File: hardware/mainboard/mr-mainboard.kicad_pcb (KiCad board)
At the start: 0 parts

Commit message: First pass at placement
Signed-off-by: David Shah <dave@ds0.me>
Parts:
- added C1: 470n, Capacitor_SMD:C_0402_1005Metric, F.Cu at (95.8, 152.2)
- added C10: 10µ, Capacitor_SMD:C_0805_2012Metric, B.Cu at (113.8, 130.0)
- added C11: 470n, Capacitor_SMD:C_0402_1005Metric, F.Cu at (89.3, 150.8)
- added C12: 10µ, Capacitor_SMD:C_0805_2012Metric, B.Cu at (113.8, 132.2)
- added C13: 10µ, Capacitor_SMD:C_0805_2012Metric, B.Cu at (113.8, 139.0)
- added C14: 10µ, Capacitor_SMD:C_0805_2012Metric, B.Cu at (81.8, 132.0)
- added C15: 10µ, Capacitor_SMD:C_0805_2012Metric, B.Cu at (83.5, 155.0)
- added C16: 10µ, Capacitor_SMD:C_0805_2012Metric, B.Cu at (81.0, 161.5)
- added C17: 10µ, Capacitor_SMD:C_0805_2012Metric, B.Cu at (83.8, 161.5)
- added C18: 10µ, Capacitor_SMD:C_0805_2012Metric, B.Cu at (92.5, 161.5)
- added C19: 10µ, Capacitor_SMD:C_0805_2012Metric, B.Cu at (86.5, 161.5)
- added C2: 470n, Capacitor_SMD:C_0402_1005Metric, F.Cu at (93.8, 152.2)
- added C20: 10µ, Capacitor_SMD:C_0805_2012Metric, B.Cu at (89.5, 161.5)
- added C21: 100n, Capacitor_SMD:C_0402_1005Metric, F.Cu at (87.8, 153.7)
- added C22: 100n, Capacitor_SMD:C_0402_1005Metric, F.Cu at (89.5, 155.8)
- added C23: 100n, Capacitor_SMD:C_0402_1005Metric, F.Cu at (90.7, 155.7)
- added C24: 100n, Capacitor_SMD:C_0402_1005Metric, F.Cu at (92.0, 155.8)
- added C25: 100n, Capacitor_SMD:C_0402_1005Metric, F.Cu at (91.0, 153.8)
- added C26: 100n, Capacitor_SMD:C_0402_1005Metric, F.Cu at (93.5, 154.5)
- added C27: 10µ, Capacitor_SMD:C_0805_2012Metric, B.Cu at (65.8, 183.0)
- added C28: 10µ, Capacitor_SMD:C_0805_2012Metric, B.Cu at (66.0, 171.8)
- added C29: 10µ, Capacitor_SMD:C_0805_2012Metric, B.Cu at (63.2, 171.8)
- added C3: 470n, Capacitor_SMD:C_0402_1005Metric, F.Cu at (94.2, 149.0)
- added C30: 100n, Capacitor_SMD:C_0402_1005Metric, F.Cu at (100.8, 149.8)
- added C31: 100n, Capacitor_SMD:C_0402_1005Metric, B.Cu at (76.3, 177.8)
- added C32: 1µ, Capacitor_SMD:C_0603_1608Metric, B.Cu at (82.5, 176.5)
- added C33: 1µ, Capacitor_SMD:C_0603_1608Metric, B.Cu at (82.5, 170.0)
- added C34: 10µ, Capacitor_SMD:C_0805_2012Metric, B.Cu at (79.0, 181.0)
- added C35: 10µ, Capacitor_SMD:C_0805_2012Metric, B.Cu at (75.0, 172.2)
- added C36: 10µ, Capacitor_SMD:C_0805_2012Metric, B.Cu at (65.8, 180.8)
- added C37: 10µ, Capacitor_SMD:C_0805_2012Metric, B.Cu at (79.0, 183.2)
- added C38: 470n, Capacitor_SMD:C_0402_1005Metric, B.Cu at (113.8, 147.5)
- added C39: 10µ, Capacitor_SMD:C_0805_2012Metric, B.Cu at (108.8, 129.5)
- added C4: 470n, Capacitor_SMD:C_0402_1005Metric, F.Cu at (95.5, 146.8)
- added C40: 10µ, Capacitor_SMD:C_0805_2012Metric, B.Cu at (81.8, 137.2)
- added C41: 10µ, Capacitor_SMD:C_0805_2012Metric, B.Cu at (83.5, 148.4)
- added C42: 470n, Capacitor_SMD:C_0402_1005Metric, F.Cu at (89.2, 145.8)
- added C43: 470n, Capacitor_SMD:C_0402_1005Metric, F.Cu at (89.2, 149.2)
- added C44: 470n, Capacitor_SMD:C_0402_1005Metric, F.Cu at (100.5, 146.5)
- added C45: 10µ, Capacitor_SMD:C_0805_2012Metric, B.Cu at (81.7, 134.8)
- added C46: 10µ, Capacitor_SMD:C_0805_2012Metric, B.Cu at (113.8, 136.8)
- added C47: 470n, Capacitor_SMD:C_0402_1005Metric, F.Cu at (93.8, 143.8)
- added C48: 470n, Capacitor_SMD:C_0402_1005Metric, F.Cu at (96.2, 150.8)
- added C49: 10µ, Capacitor_SMD:C_0805_2012Metric, B.Cu at (113.8, 134.5)
- added C5: 470n, Capacitor_SMD:C_0402_1005Metric, F.Cu at (97.0, 142.8)
- added C50: 470n, Capacitor_SMD:C_0402_1005Metric, F.Cu at (92.8, 142.8)
- added C51: 470n, Capacitor_SMD:C_0402_1005Metric, F.Cu at (89.0, 142.0)
- added C52: 470n, Capacitor_SMD:C_0402_1005Metric, F.Cu at (99.0, 142.5)
- added C53: 470n, Capacitor_SMD:C_0402_1005Metric, F.Cu at (89.2, 148.0)
- added C54: 470n, Capacitor_SMD:C_0402_1005Metric, F.Cu at (93.0, 146.8)
- added C55: 10µ, Capacitor_SMD:C_0805_2012Metric, B.Cu at (74.5, 142.5)
- added C56: 10µ, Capacitor_SMD:C_0805_2012Metric, B.Cu at (74.5, 161.0)
- added C57: 10µ, Capacitor_SMD:C_0805_2012Metric, B.Cu at (77.0, 161.0)
- added C58: 10µ, Capacitor_SMD:C_0805_2012Metric, B.Cu at (77.0, 142.5)
- added C59: 10µ, Capacitor_SMD:C_0805_2012Metric, B.Cu at (77.0, 152.5)
- added C6: 470n, Capacitor_SMD:C_0402_1005Metric, F.Cu at (98.0, 151.5)
- added C60: 10µ, Capacitor_SMD:C_0805_2012Metric, B.Cu at (74.5, 152.5)
- added C61: 10µ, Capacitor_SMD:C_0805_2012Metric, B.Cu at (71.5, 147.4)
- added C62: 10µ, Capacitor_SMD:C_0805_2012Metric, B.Cu at (70.0, 166.5)
- added C63: 10µ, Capacitor_SMD:C_0805_2012Metric, B.Cu at (69.0, 156.5)
- added C64: 10µ, Capacitor_SMD:C_0805_2012Metric, B.Cu at (69.0, 147.4)
- added C65: 10µ, Capacitor_SMD:C_0805_2012Metric, B.Cu at (72.5, 166.6)
- added C66: 10µ, Capacitor_SMD:C_0805_2012Metric, B.Cu at (71.5, 156.5)
- added C67: 470n, Capacitor_SMD:C_0402_1005Metric, F.Cu at (98.2, 153.0)
- added C68: 470n, Capacitor_SMD:C_0402_1005Metric, B.Cu at (107.8, 115.2)
- added C69: 100n, Capacitor_SMD:C_0402_1005Metric, B.Cu at (111.2, 119.3)
- added C7: 470n, Capacitor_SMD:C_0402_1005Metric, F.Cu at (94.2, 150.5)
- added C70: 470n, Capacitor_SMD:C_0402_1005Metric, F.Cu at (96.8, 149.0)
- added C71: 100n, Capacitor_SMD:C_0402_1005Metric, F.Cu at (97.8, 154.2)
- added C72: 10µ, Capacitor_SMD:C_0805_2012Metric, B.Cu at (97.5, 161.5)
- added C73: 100n, Capacitor_SMD:C_0402_1005Metric, F.Cu at (95.5, 155.8)
- added C74: 10µ, Capacitor_SMD:C_0805_2012Metric, B.Cu at (100.0, 161.5)
- added C75: 100n, Capacitor_SMD:C_0402_1005Metric, F.Cu at (98.6, 155.8)
- added C76: 100n, Capacitor_SMD:C_0402_1005Metric, F.Cu at (100.0, 155.8)
- added C77: 2.2µ, Capacitor_SMD:C_0603_1608Metric, B.Cu at (94.8, 161.5)
- added C78: 12p, Capacitor_SMD:C_0402_1005Metric, F.Cu at (113.0, 183.0)
- added C79: 470n, Capacitor_SMD:C_0402_1005Metric, F.Cu at (118.5, 179.8)
- added C8: 470n, Capacitor_SMD:C_0402_1005Metric, F.Cu at (97.5, 147.2)
- added C80: 470n, Capacitor_SMD:C_0402_1005Metric, F.Cu at (125.2, 182.0)
- added C81: 12p, Capacitor_SMD:C_0402_1005Metric, F.Cu at (117.5, 183.0)
- added C82: 470n, Capacitor_SMD:C_0402_1005Metric, F.Cu at (91.2, 125.2)
- added C83: 470n, Capacitor_SMD:C_0402_1005Metric, F.Cu at (93.5, 125.2)
- added C84: 470n, Capacitor_SMD:C_0402_1005Metric, F.Cu at (101.2, 125.2)
- added C85: 470n, Capacitor_SMD:C_0402_1005Metric, F.Cu at (94.7, 127.2)
- added C86: 470n, Capacitor_SMD:C_0402_1005Metric, F.Cu at (95.0, 121.8)
- added C87: 470n, Capacitor_SMD:C_0402_1005Metric, F.Cu at (101.2, 126.5)
- added C88: 470n, Capacitor_SMD:C_0402_1005Metric, F.Cu at (99.2, 125.2)
- added C89: 470n, Capacitor_SMD:C_0402_1005Metric, F.Cu at (90.2, 132.8)
- added C9: 470n, Capacitor_SMD:C_0402_1005Metric, F.Cu at (101.8, 143.7)
- added C90: 470n, Capacitor_SMD:C_0402_1005Metric, F.Cu at (93.0, 132.8)
- added C91: 470n, Capacitor_SMD:C_0402_1005Metric, F.Cu at (101.0, 132.8)
- added C92: 470n, Capacitor_SMD:C_0402_1005Metric, F.Cu at (98.5, 132.8)
- added CAM1: PI_CAM_22P, meowality:54548-2271, B.Cu at (96.0, 186.0)
- added D1: LED_ABGR, LED_SMD:LED_Cree-PLCC4_2x2mm_CW, B.Cu at (127.5, 102.0)
- added D2: LED_ABGR, LED_SMD:LED_Cree-PLCC4_2x2mm_CW, B.Cu at (127.5, 107.0)
- added D3: LED_ABGR, LED_SMD:LED_Cree-PLCC4_2x2mm_CW, B.Cu at (122.0, 102.0)
- added D4: LED_ABGR, LED_SMD:LED_Cree-PLCC4_2x2mm_CW, B.Cu at (62.5, 102.0)
- added D5: LED_Small, LED_SMD:LED_0805_2012Metric, B.Cu at (68.5, 107.0)
- added D6: LED_ABGR, LED_SMD:LED_Cree-PLCC4_2x2mm_CW, B.Cu at (62.5, 107.0)
- added D7: LED_ABGR, LED_SMD:LED_Cree-PLCC4_2x2mm_CW, B.Cu at (68.5, 102.0)
- added D8: LED_Small, LED_SMD:LED_0805_2012Metric, B.Cu at (122.0, 107.0)
- added FB1: 120, Inductor_SMD:L_0603_1608Metric, B.Cu at (80.8, 155.0)
- added FB10: 120, Inductor_SMD:L_0603_1608Metric, F.Cu at (125.2, 179.5)
- added FB2: 120, Inductor_SMD:L_0603_1608Metric, B.Cu at (81.0, 165.0)
- added FB3: 120, Inductor_SMD:L_0603_1608Metric, B.Cu at (83.8, 165.0)
- added FB4: 120, Inductor_SMD:L_0603_1608Metric, B.Cu at (92.5, 165.0)
- added FB5: 120, Inductor_SMD:L_0603_1608Metric, B.Cu at (86.5, 165.0)
- added FB6: 120, Inductor_SMD:L_0603_1608Metric, B.Cu at (89.5, 165.0)
- added FB7: 120, Inductor_SMD:L_0603_1608Metric, B.Cu at (94.8, 165.0)
- added FB8: 120, Inductor_SMD:L_0603_1608Metric, B.Cu at (97.5, 165.0)
- added FB9: 120, Inductor_SMD:L_0603_1608Metric, B.Cu at (100.0, 165.0)
- added J1: Conn_01x40_Shielded, meowality:TE_FPC_40pin_p0.5mm_4-1734839-0, B.Cu at (124.0, 123.0)
- added J2: Conn_01x40_Shielded, meowality:TE_FPC_40pin_p0.5mm_4-1734839-0, B.Cu at (66.0, 123.0)
- added J3: EAR, Connector_PinHeader_2.54mm:PinHeader_2x03_P2.54mm_Horizontal, F.Cu at (28.0, 121.0)
- added J4: Conn_02x06_Top_Bottom, Connector_PinSocket_2.54mm:PinSocket_2x06_P2.54mm_Horizontal, F.Cu at (95.5, 113.0)
- added L1: XFL3012-103MEB, meowality:XFL3012, B.Cu at (65.8, 176.8)
- added L2: XFL4020-472MEB, Inductor_SMD:L_Coilcraft_XxL4020, B.Cu at (70.5, 171.8)
- added L3: XFL4020-472MEB, Inductor_SMD:L_Coilcraft_XxL4020, B.Cu at (72.0, 183.0)
- added L4: XFL4015-471MEB, Inductor_SMD:L_Coilcraft_XxL4020, B.Cu at (65.0, 144.8)
- added L5: XFL4015-471MEB, Inductor_SMD:L_Coilcraft_XxL4020, B.Cu at (65.0, 161.5)
- added L6: XFL4015-471MEB, Inductor_SMD:L_Coilcraft_XxL4020, B.Cu at (65.0, 154.2)
- added LCD1: H381Dxx0y.z, meowality:FH35C-39S-0.3SHW, F.Cu at (97.0, 183.0)
- added P1: M2_SOCKET_E, meowality:2199230-4, B.Cu at (118.0, 185.0)
- added Q1: 2N7002, Package_TO_SOT_SMD:SOT-23, F.Cu at (117.6, 123.0)
- added R1: 0, Resistor_SMD:R_0402_1005Metric, B.Cu at (76.2, 176.2)
- added R10: 10k, Resistor_SMD:R_0402_1005Metric, B.Cu at (70.5, 151.0)
- added R11: 6.98k, Resistor_SMD:R_0402_1005Metric, B.Cu at (74.0, 146.5)
- added R12: 10k, Resistor_SMD:R_0402_1005Metric, B.Cu at (74.0, 148.0)
- added R13: 20k, Resistor_SMD:R_0402_1005Metric, B.Cu at (75.0, 166.0)
- added R14: 10k, Resistor_SMD:R_0402_1005Metric, B.Cu at (75.0, 167.5)
- added R15: 15k, Resistor_SMD:R_0402_1005Metric, B.Cu at (74.0, 155.5)
- added R16: 10k, Resistor_SMD:R_0402_1005Metric, B.Cu at (74.0, 157.0)
- added R17: 10k, Resistor_SMD:R_0402_1005Metric, B.Cu at (80.2, 127.0)
- added R18: 1k, Resistor_SMD:R_0402_1005Metric, F.Cu at (68.5, 107.0)
- added R19: 10k, Resistor_SMD:R_0402_1005Metric, F.Cu at (117.5, 118.5)
- added R2: 10k, Resistor_SMD:R_0402_1005Metric, F.Cu at (94.2, 186.5)
- added R20: 220, Resistor_SMD:R_0402_1005Metric, F.Cu at (65.5, 102.8)
- added R21: 220, Resistor_SMD:R_0402_1005Metric, F.Cu at (65.5, 104.2)
- added R22: 220, Resistor_SMD:R_0402_1005Metric, F.Cu at (65.5, 105.8)
- added R23: 1k, Resistor_SMD:R_0402_1005Metric, B.Cu at (119.8, 109.8)
- added R24: 1.15k, Resistor_SMD:R_0402_1005Metric, F.Cu at (97.5, 155.7)
- added R25: 10k, Resistor_SMD:R_0402_1005Metric, F.Cu at (64.5, 130.8)
- added R26: 10k, Resistor_SMD:R_0402_1005Metric, F.Cu at (105.5, 109.8)
- added R27: 10k, Resistor_SMD:R_0402_1005Metric, F.Cu at (137.5, 74.8)
- added R28: 10k, Resistor_SMD:R_0402_1005Metric, F.Cu at (116.5, 109.8)
- added R29: 10k, Resistor_SMD:R_0402_1005Metric, F.Cu at (113.5, 179.8)
- added R3: 4.7k, Resistor_SMD:R_0402_1005Metric, F.Cu at (106.5, 153.8)
- added R30: NC, Resistor_SMD:R_0402_1005Metric, F.Cu at (96.2, 132.8)
- added R31: 1k, Resistor_SMD:R_0402_1005Metric, F.Cu at (96.2, 121.8)
- added R32: 1k, Resistor_SMD:R_0402_1005Metric, F.Cu at (93.8, 121.8)
- added R33: 10k, Resistor_SMD:R_0402_1005Metric, B.Cu at (110.5, 111.8)
- added R4: 4.7k, Resistor_SMD:R_0402_1005Metric, F.Cu at (96.2, 159.5)
- added R5: 4.7k, Resistor_SMD:R_0402_1005Metric, F.Cu at (106.5, 151.5)
- added R6: 4.7k, Resistor_SMD:R_0402_1005Metric, F.Cu at (64.5, 127.0)
- added R7: 4.7k, Resistor_SMD:R_0402_1005Metric, B.Cu at (75.0, 115.5)
- added R8: 10k, Resistor_SMD:R_0402_1005Metric, B.Cu at (70.5, 141.0)
- added R9: 10k, Resistor_SMD:R_0402_1005Metric, B.Cu at (70.5, 160.5)
- added SW1: SW_Push, Button_Switch_THT:SW_Tactile_SPST_Angled_PTS645Vx31-2LFS, F.Cu at (100.5, 103.0)
- added SW2: SW_Push, Button_Switch_THT:SW_Tactile_SPST_Angled_PTS645Vx31-2LFS, F.Cu at (150.5, 93.5)
- added SW3: SW_Push, Button_Switch_THT:SW_Tactile_SPST_Angled_PTS645Vx31-2LFS, F.Cu at (111.0, 103.0)
- added TP1: TestPoint, TestPoint:TestPoint_Pad_D2.0mm, F.Cu at (94.0, 173.0)
- added U1: LIFCL_40_CABGA400, meowality:BGA-400_20x20_17.0x17.0mm, B.Cu at (95.0, 148.5)
- added U10: Si52112-B, meowality:TDFN10_3x3mm_p0.5mm, F.Cu at (120.0, 182.0)
- added U11: EM6GA16LBXA-12H, Package_BGA:BGA-96_9.0x13.0mm_Layout2x3x16_P0.8mm, B.Cu at (95.2, 128.8)
- added U2: TPS65632R, Package_DFN_QFN:QFN-16-1EP_3x3mm_P0.5mm_EP1.7x1.7mm, B.Cu at (71.8, 177.8)
- added U3: TLV71330PDBV, Package_TO_SOT_SMD:SOT-23-5, B.Cu at (82.5, 173.2)
- added U4: TPS62822, meowality:TI_VSON-HR_1.5x2mm_p0.5mm, B.Cu at (70.5, 143.5)
- added U5: TPS62822, meowality:TI_VSON-HR_1.5x2mm_p0.5mm, B.Cu at (70.5, 163.0)
- added U6: TPS62822, meowality:TI_VSON-HR_1.5x2mm_p0.5mm, B.Cu at (70.5, 153.5)
- added U7: W25Q128JVS, Package_SO:SOIC-8_5.23x5.23mm_P1.27mm, B.Cu at (80.0, 121.0)
- added U8: ICM-20948, Sensor_Motion:InvenSense_QFN-24_3x3mm_P0.4mm, B.Cu at (111.5, 115.2)
- added U9: 74AHC1G126, Package_TO_SOT_SMD:SOT-23-5, B.Cu at (74.0, 132.9)
- added X1: XO32, Oscillator:Oscillator_SMD_EuroQuartz_XO32-4Pin_3.2x2.5mm, B.Cu at (113.7, 143.6)
- added Y1: 25MHz, Crystal:Crystal_SMD_2016-4Pin_2.0x1.6mm, F.Cu at (115.2, 183.1)
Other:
- board outline added: 70 x 90 mm
- copper layers 0 -> 2

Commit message: Working on layout
Signed-off-by: David Shah <dave@ds0.me>
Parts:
- removed R27: 10k, Resistor_SMD:R_0402_1005Metric
- removed the SW2 at (150.5, 93.5)
- added H1: MountingHole, MountingHole:MountingHole_2.7mm_M2.5, F.Cu at (125.0, 142.0)
- added H2: MountingHole, MountingHole:MountingHole_2.7mm_M2.5, F.Cu at (64.0, 186.0)
- added H3: MountingHole, MountingHole:MountingHole_2.7mm_M2.5, F.Cu at (101.5, 113.5)
- added H4: MountingHole, MountingHole:MountingHole_2.7mm_M2.5, F.Cu at (124.5, 172.0)
- added H5: MountingHole, meowality:9774025151R, F.Cu at (118.0, 153.2)
- J3: footprint Connector_PinHeader_2.54mm:PinHeader_2x03_P2.54mm_Horizontal -> Connector_PinHeader_2.00mm:PinHeader_2x03_P2.00mm_Horizontal
- moved J3 46.8 mm to (73.5, 110.0)
- moved FB2 10.8 mm to (81.0, 154.2), turned to 180 degrees
- moved FB3 5.96 mm to (81.0, 159.8), turned to 180 degrees
- moved C16 5.50 mm to (81.0, 156.0), turned to 0 degrees
- moved C72 5.35 mm to (101.5, 165.0), turned to 0 degrees
- moved FB5 5.27 mm to (82.0, 162.3)
- moved C38 5.14 mm to (117.0, 143.5), turned to -90 degrees
- moved C15 4.74 mm to (81.0, 151.0), turned to 0 degrees
- moved C17 4.45 mm to (81.0, 158.0), turned to 0 degrees
- moved FB8 4.33 mm to (101.5, 166.8), turned to 0 degrees
- moved C20 3.87 mm to (85.8, 162.4)
- moved FB4 3.69 mm to (90.0, 162.3)
- moved FB6 3.40 mm to (87.5, 162.3)
- moved C71 3.11 mm to (96.3, 157.0), turned to 90 degrees
- moved C19 2.91 mm to (83.8, 162.4)
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- renumbered SW3 to SW2
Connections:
- R28 pad 1: BTN2 -> BTN1
- SW2 pad 2: BTN2 -> BTN1
- U1 pad R2: BTN_2 -> unconnected-(U1-PadR2)
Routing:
- net GND: track 0.00 -> 37.1 mm, vias 0 -> 42
- net +3V3: track 0.00 -> 30.2 mm, vias 0 -> 5
- net +1V8: track 0.00 -> 17.2 mm, vias 0 -> 11
- net +1V0: track 0.00 -> 13.1 mm, vias 0 -> 8
- net +1V5: track 0.00 -> 10.1 mm, vias 0 -> 2
- net Net-(R13-Pad2): track 0.00 -> 6.90 mm
- net Net-(R15-Pad2): track 0.00 -> 6.89 mm
- net Net-(R11-Pad2): track 0.00 -> 6.60 mm
- net Net-(L6-Pad1): track 0.00 -> 5.42 mm
- net Net-(L5-Pad1): track 0.00 -> 5.21 mm
- net Net-(L4-Pad1): track 0.00 -> 5.21 mm
- net Net-(C74-Pad1): track 0.00 -> 2.72 mm, vias 0 -> 2
- net Net-(C19-Pad2): track 0.00 -> 1.74 mm, vias 0 -> 1
- net Net-(C20-Pad2): track 0.00 -> 1.47 mm, vias 0 -> 1
- net Net-(C18-Pad2): track 0.00 -> 1.34 mm, vias 0 -> 1
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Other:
- copper layers 2 -> 6
- board text added: "Meowality"

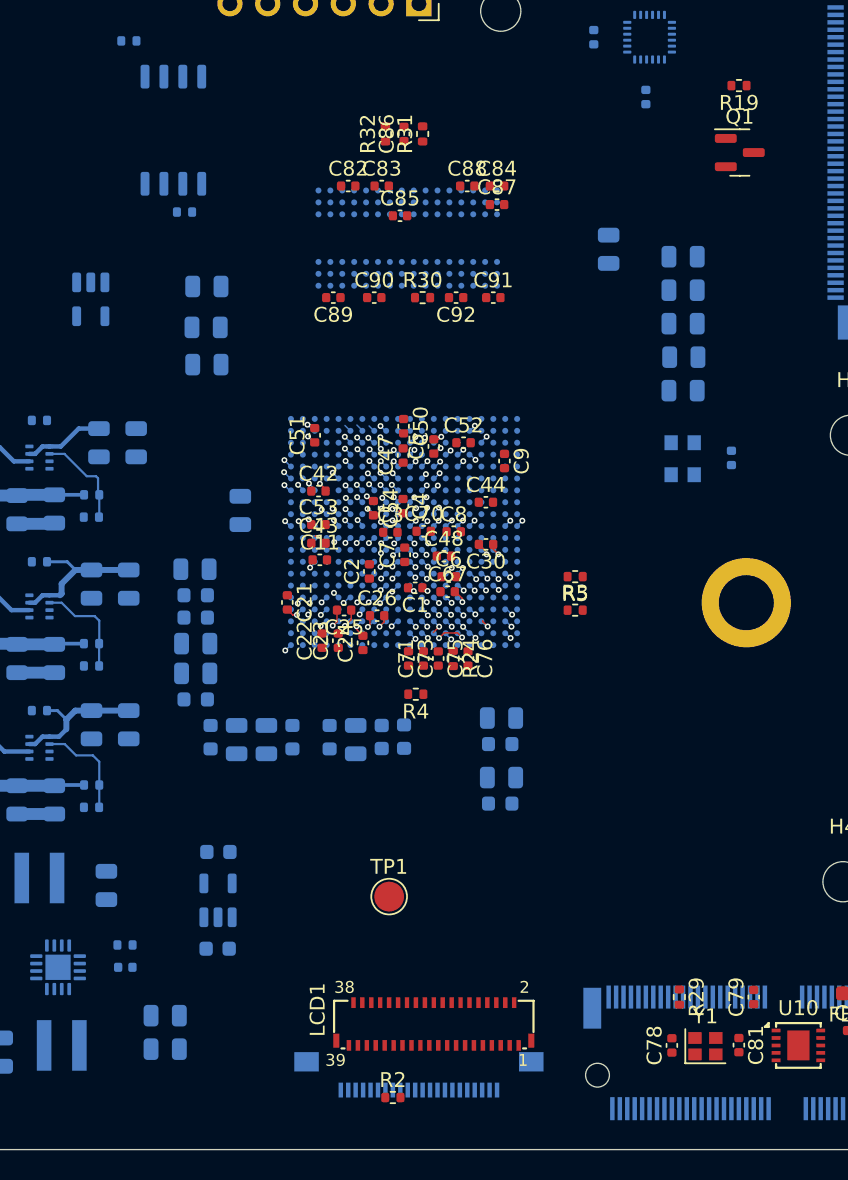
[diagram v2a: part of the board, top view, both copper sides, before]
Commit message: MIPI routing
Signed-off-by: David Shah <dave@ds0.me>
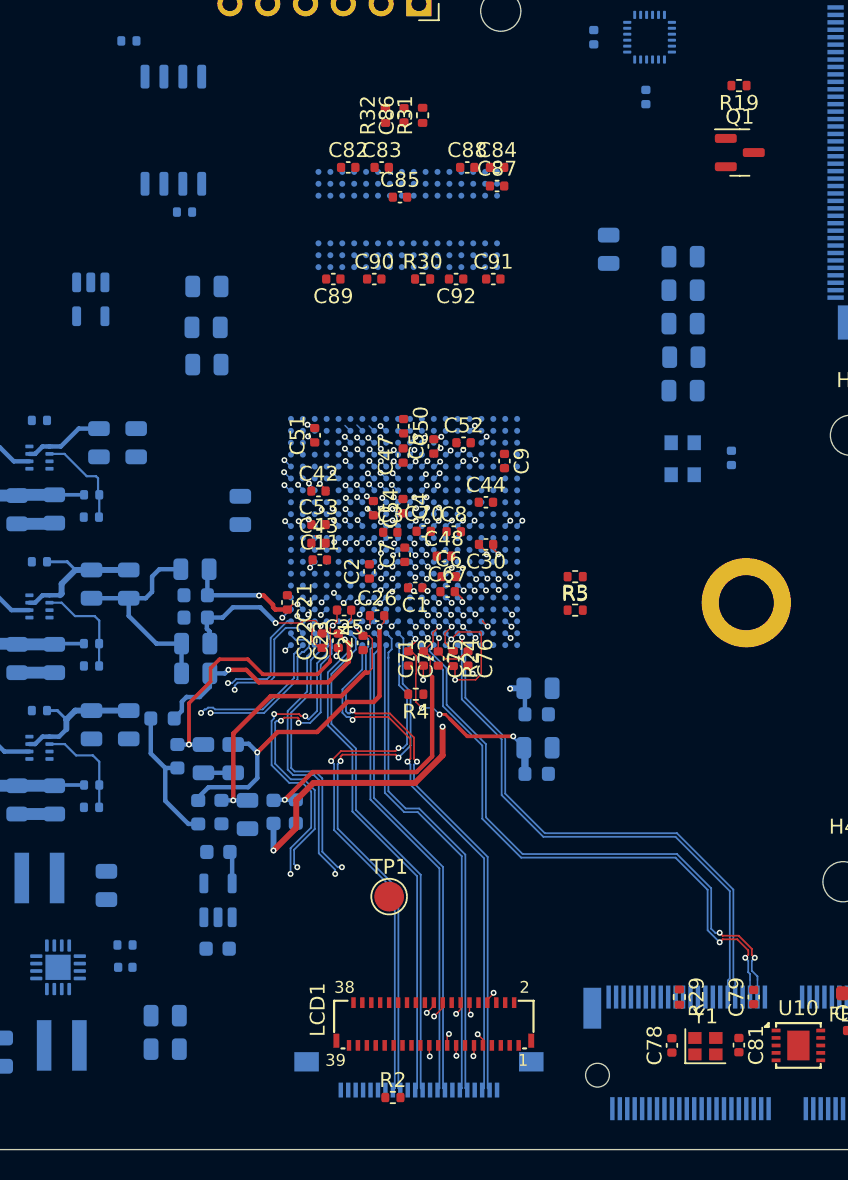
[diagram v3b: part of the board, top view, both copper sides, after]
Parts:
- moved J1 58.0 mm to (66.0, 123.0), turned to 90 degrees
- moved J2 58.0 mm to (124.0, 123.0), turned to -90 degrees
- moved C18 8.84 mm to (84.5, 167.5)
- moved C77 8.84 mm to (86.2, 167.3)
- moved FB4 8.84 mm to (82.7, 167.3)
- moved FB7 8.84 mm to (87.7, 167.3)
- moved FB6 8.09 mm to (81.2, 167.3)
- moved C72 3.16 mm to (104.0, 163.0)
- moved C74 3.16 mm to (104.0, 159.0)
- moved FB8 3.16 mm to (103.9, 164.8)
- moved FB9 3.16 mm to (103.9, 160.8)
- moved C19 2.57 mm to (81.5, 163.7)
- moved C20 2.57 mm to (83.5, 163.7)
- moved FB3 2.57 mm to (78.8, 161.0)
- moved FB5 2.57 mm to (79.8, 163.6)
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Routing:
- net /Cam_Disp/DISP_CK+: track 0.00 -> 48.3 mm, vias 0 -> 2
- net /Cam_Disp/DISP_D0-: track 0.00 -> 47.9 mm, vias 0 -> 2
- net /Cam_Disp/DISP_CK-: track 0.00 -> 47.0 mm, vias 0 -> 2
- net /Cam_Disp/DISP_D2+: track 0.00 -> 46.0 mm, vias 0 -> 2
- net /Cam_Disp/DISP_D0+: track 0.00 -> 45.5 mm, vias 0 -> 2
- net /Cam_Disp/DISP_D2-: track 0.00 -> 42.7 mm, vias 0 -> 2
- net /Cam_Disp/DISP_D3+: track 0.00 -> 41.5 mm, vias 0 -> 4
- net M2_RX0-: track 0.00 -> 40.0 mm, vias 0 -> 2
- net M2_RX0+: track 0.00 -> 39.9 mm, vias 0 -> 2
- net /Cam_Disp/DISP_D3-: track 0.00 -> 39.3 mm, vias 0 -> 4
- net /Cam_Disp/CAM_D0-: track 0.00 -> 37.5 mm, vias 0 -> 2
- net /Cam_Disp/CAM_D3-: track 0.00 -> 37.3 mm, vias 0 -> 2
- net /Cam_Disp/DISP_D1-: track 0.00 -> 37.0 mm, vias 0 -> 2
- net M2_TX0-: track 0.00 -> 36.5 mm
- net M2_TX0+: track 0.00 -> 36.5 mm
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
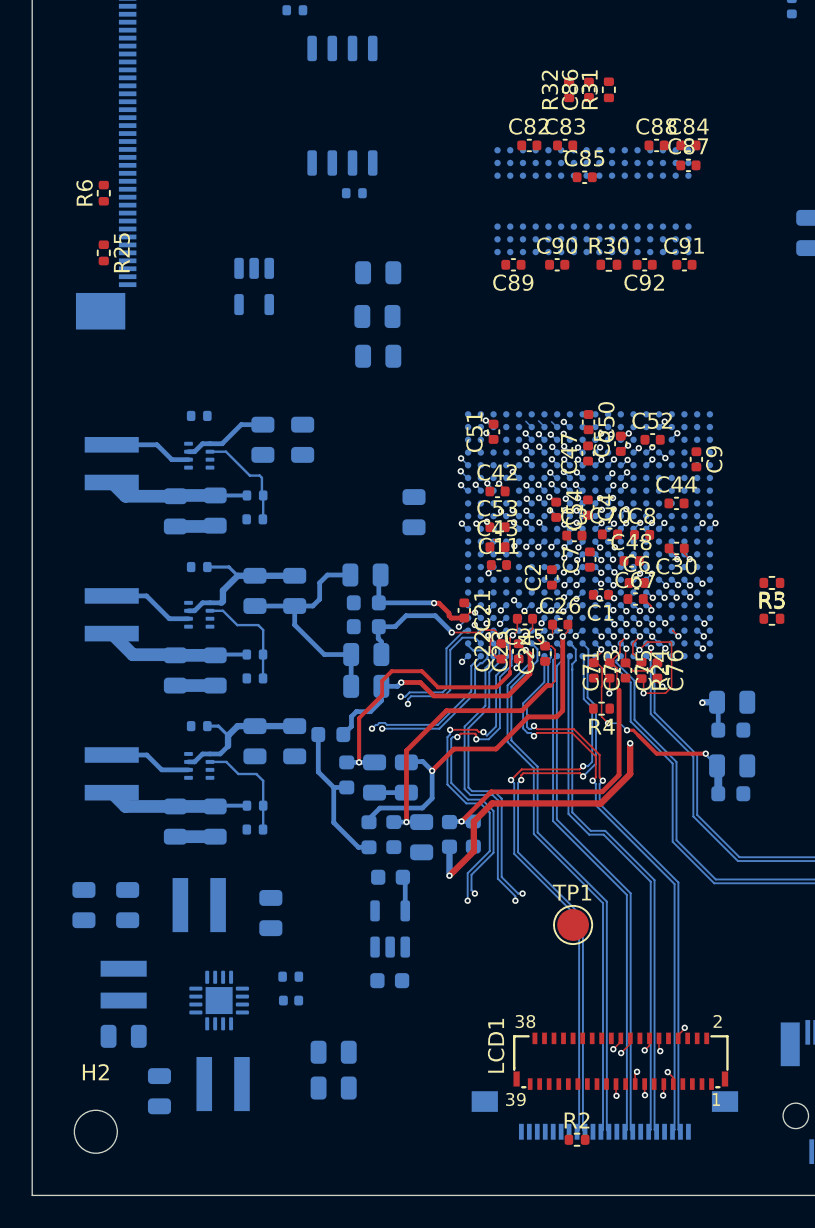
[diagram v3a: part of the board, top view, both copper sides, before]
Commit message: DRAM routing
Signed-off-by: David Shah <dave@ds0.me>
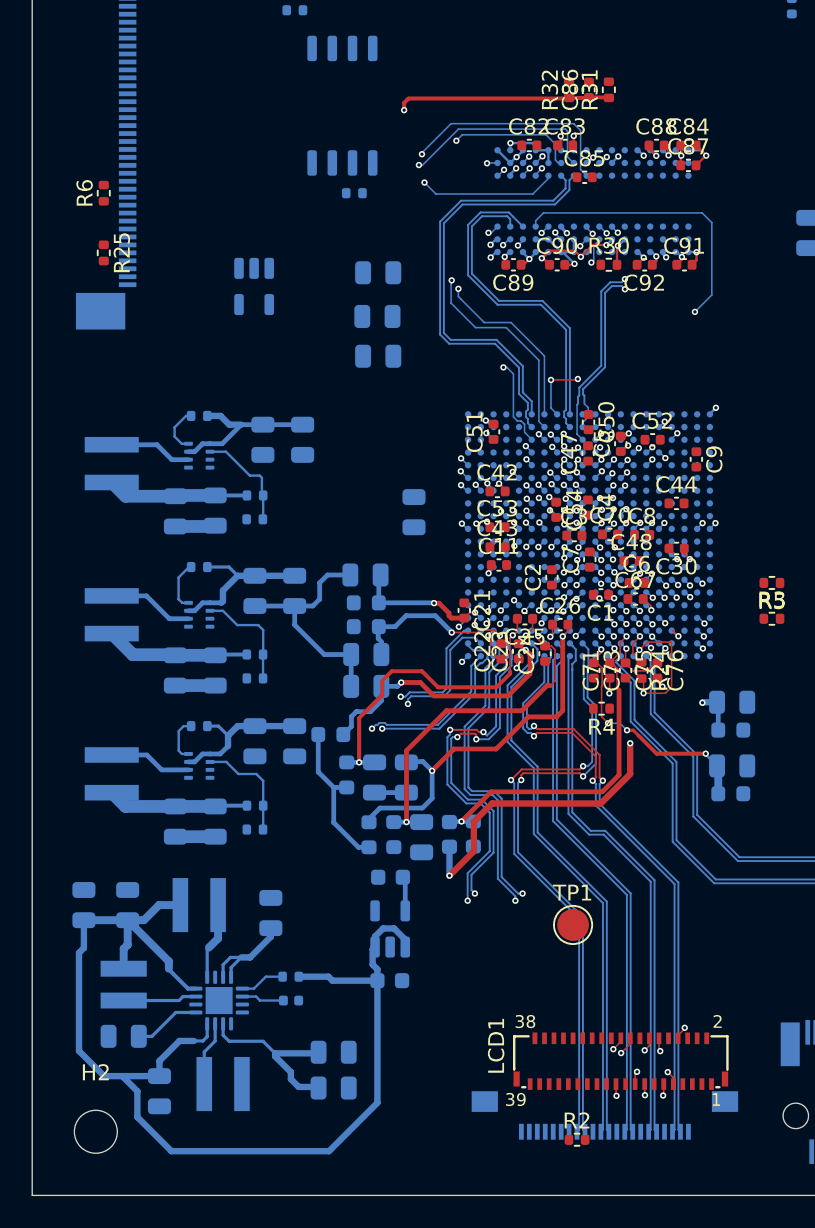
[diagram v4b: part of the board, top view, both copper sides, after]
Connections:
- U1 pad P10: RAM_DQ9 -> RAM_DQ7
- U1 pad P7: RAM_DQ5 -> RAM_DQ8
- U1 pad P8: RAM_DQ6 -> RAM_DQ11
- U1 pad P9: RAM_DQ8 -> RAM_DQ3
- U1 pad R10: RAM_DQ10 -> RAM_DQ5
- U1 pad R11: unconnected-(U1-PadR11) -> RAM_DQ2
- U1 pad R8: RAM_DQ7 -> RAM_DQ10
- U1 pad T10: RAM_DQ13 -> RAM_DQ4
- U1 pad T11: RAM_DQ14 -> RAM_DQ6
- U1 pad T8: RAM_CLK+ -> unconnected-(U1-PadT8)
- U1 pad U10: RAM_DQ15 -> RAM_DQ0
- U1 pad U6: RAM_DQ0 -> RAM_DQ9
- U1 pad U7: RAM_DQ2 -> unconnected-(U1-PadU7)
- U1 pad V10: unconnected-(U1-PadV10) -> RAM_CLK+
- U1 pad V6: RAM_DQ1 -> RAM_DQ13
- U1 pad V7: RAM_DQ4 -> RAM_DQ15
- U1 pad V9: RAM_DQ12 -> RAM_DQ1
- U1 pad W10: unconnected-(U1-PadW10) -> RAM_CLK-
- U1 pad W6: RAM_DSQ0+ -> RAM_DQS1+
- U1 pad W7: RAM_DQ3 -> RAM_DQ12
- U1 pad W8: RAM_DQ11 -> unconnected-(U1-PadW8)
- U1 pad W9: RAM_DSQ1+ -> RAM_DQS0+
- U1 pad Y6: RAM_DSQ0- -> RAM_DQS1-
- U1 pad Y7: RAM_CLK- -> RAM_DQ14
- U1 pad Y9: RAM_DSQ1- -> RAM_DQS0-
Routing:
- net +3V3: track 30.2 -> 109.2 mm
- net RAM_VREF: track 0.51 -> 48.0 mm, vias 1 -> 2
- net RAM_DQ11: track 0.49 -> 46.2 mm, vias 0 -> 2
- net RAM_DQ8: track 0.53 -> 44.3 mm, vias 1 -> 2
- net RAM_DQ9: track 0.57 -> 42.0 mm, vias 1 -> 2
- net RAM_DQ6: track 0.55 -> 38.3 mm, vias 1 -> 2
- net RAM_DQ10: track 0.50 -> 37.7 mm, vias 1 -> 2
- net RAM_DQ7: track 0.57 -> 35.5 mm, vias 1 -> 2
- net RAM_DQ2: track 0.50 -> 32.8 mm, vias 1 -> 2
- net RAM_DQ5: track 0.52 -> 32.2 mm, vias 1 -> 2
- net RAM_DQ12: track 0.54 -> 30.5 mm, vias 1 -> 2
- net RAM_DQ4: track 0.49 -> 30.3 mm, vias 1 -> 2
- net RAM_DQ14: track 0.52 -> 28.5 mm, vias 1 -> 2
- net RAM_DQS1+: track 0.00 -> 26.8 mm
- net RAM_~CS: track 0.00 -> 26.7 mm, vias 0 -> 3
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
